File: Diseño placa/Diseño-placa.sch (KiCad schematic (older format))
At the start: 71 parts, among them M0 DIL24, M1 DIL24, M2 DIL16, SW1 SW_PUSH, SW2 SW_PUSH, SW3 SW_PUSH, SW4 SW_PUSH, SW5 SW_PUSH, U1 OPA625, U2 OPA625, U3 OPA625, U4 OPA625, U5 OPA625, U6 OPA625, X1 16M

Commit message: Más esquemático Kicad
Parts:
- added C28: 0.1u, symbol C
- added C29: 10n, symbol C
- added C30: 10u, symbol CP1
- added P1: CONN_02X08, symbol CONN_02X08
- added P?: CONN_01X01, symbol CONN_01X01
- added RV1: POT, symbol POT
- added U? (x2): REG104, symbol REG104
- gave numbers to parts that had none: 1
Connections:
- net VCC is gone; now on net GND: C11.2, C12.1, C15.1, C17.2, C22.2, C25.2, C4.1, DS1.2 (VDD), IC?.10 (VCC), IC?.30 (AVCC), M0.24 (P24), M1.24 (P24), M2.16, R27.1, R28.1
- net GND: now also DS1.15 (LED+), DS1.16 (LED-), C28.2, C29.2, C30.1, C30.2, RV1.1, RV1.2, RV1.3, U?.1 (OUT), U?.1 (OUT), U?.3 (GND), U?.3 (GND)
- net LCDE: now also DS1.6 (E)
- net LCDRS: now also DS1.4 (RS)
- net LCDRW: now also DS1.5 (R/W)
- net E15: now reaches M0.16 (P16)
- net E15: now also M1.16 (P16), P1.16 (P16)
- net E14: now reaches M0.17 (P17)
- net E14: now also M1.17 (P17), P1.14 (P14)
- net E13: now reaches M0.18 (P18)
- net E13: now also M1.18 (P18), P1.12 (P12)
- net E12: now reaches M0.19 (P19)
- net E12: now also M1.19 (P19), P1.10 (P10)
- net E7: now reaches M0.2 (P2)
- net E7: now also M1.2 (P2), P1.1 (P1)
- net E11: now reaches M0.20 (P20)
- net E11: now also M1.20 (P20), P1.8 (P8)
- net E10: now reaches M0.21 (P21)
- net E10: now also M1.21 (P21), P1.6 (P6)
- net E9: now reaches M0.22 (P22)
- net E9: now also M1.22 (P22), P1.4 (P4)
- net E8: now reaches M0.23 (P23)
- net E8: now also M1.23 (P23), P1.2 (P2)
- net E6: now reaches M0.3 (P3)
- net E6: now also M1.3 (P3), P1.3 (P3)
- net E5: now reaches M0.4 (P4)
- net E5: now also M1.4 (P4), P1.5 (P5)
- net E4: now reaches M0.5 (P5)
- net E4: now also M1.5 (P5), P1.7 (P7)
- net E3: now reaches M0.6 (P6)
- net E3: now also M1.6 (P6), P1.9 (P9)
- net E2: now reaches M0.7 (P7)
- net E2: now also M1.7 (P7), P1.11 (P11)
- net E1: now reaches M0.8 (P8)
- net E1: now also M1.8 (P8), P1.13 (P13)
- net E0: now reaches M0.9 (P9)
- net E0: now also M1.9 (P9), P1.15 (P15)
- new net: C29.1, U?.2 (NR), U?.2 (NR)
- new net: C28.1, P?.1 (P1), U?.4 (ENABLE), U?.4 (ENABLE), U?.5 (IN), U?.5 (IN)

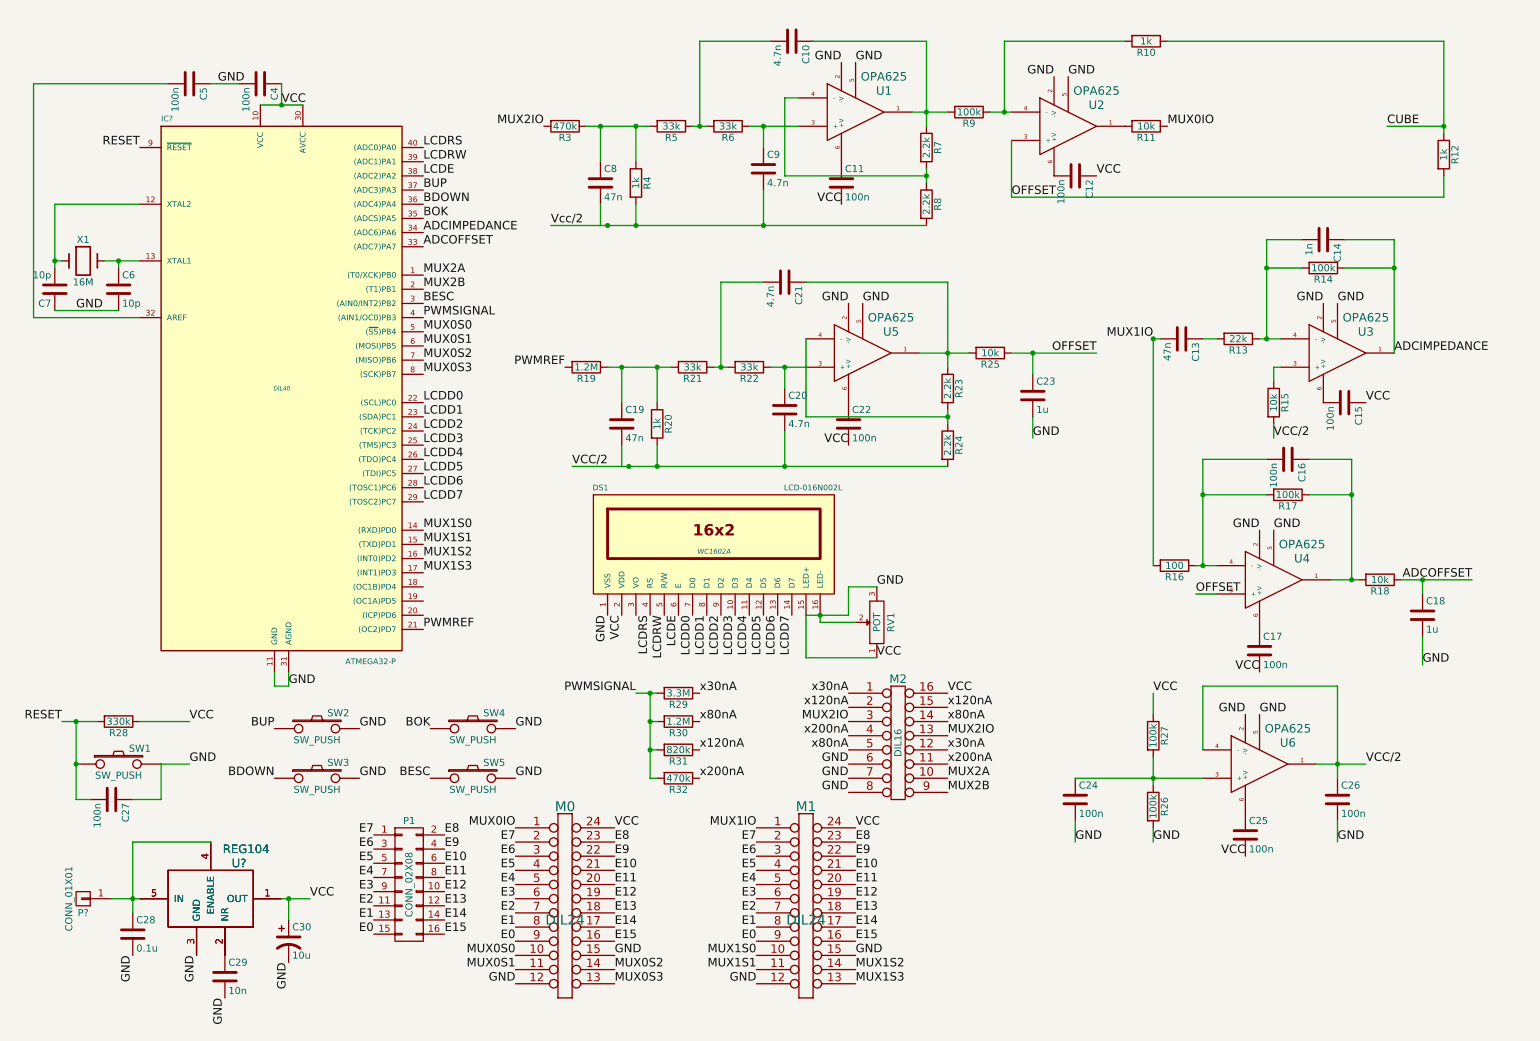
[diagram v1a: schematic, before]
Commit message: Correcciones esquemático y asociación de componentes Kicad
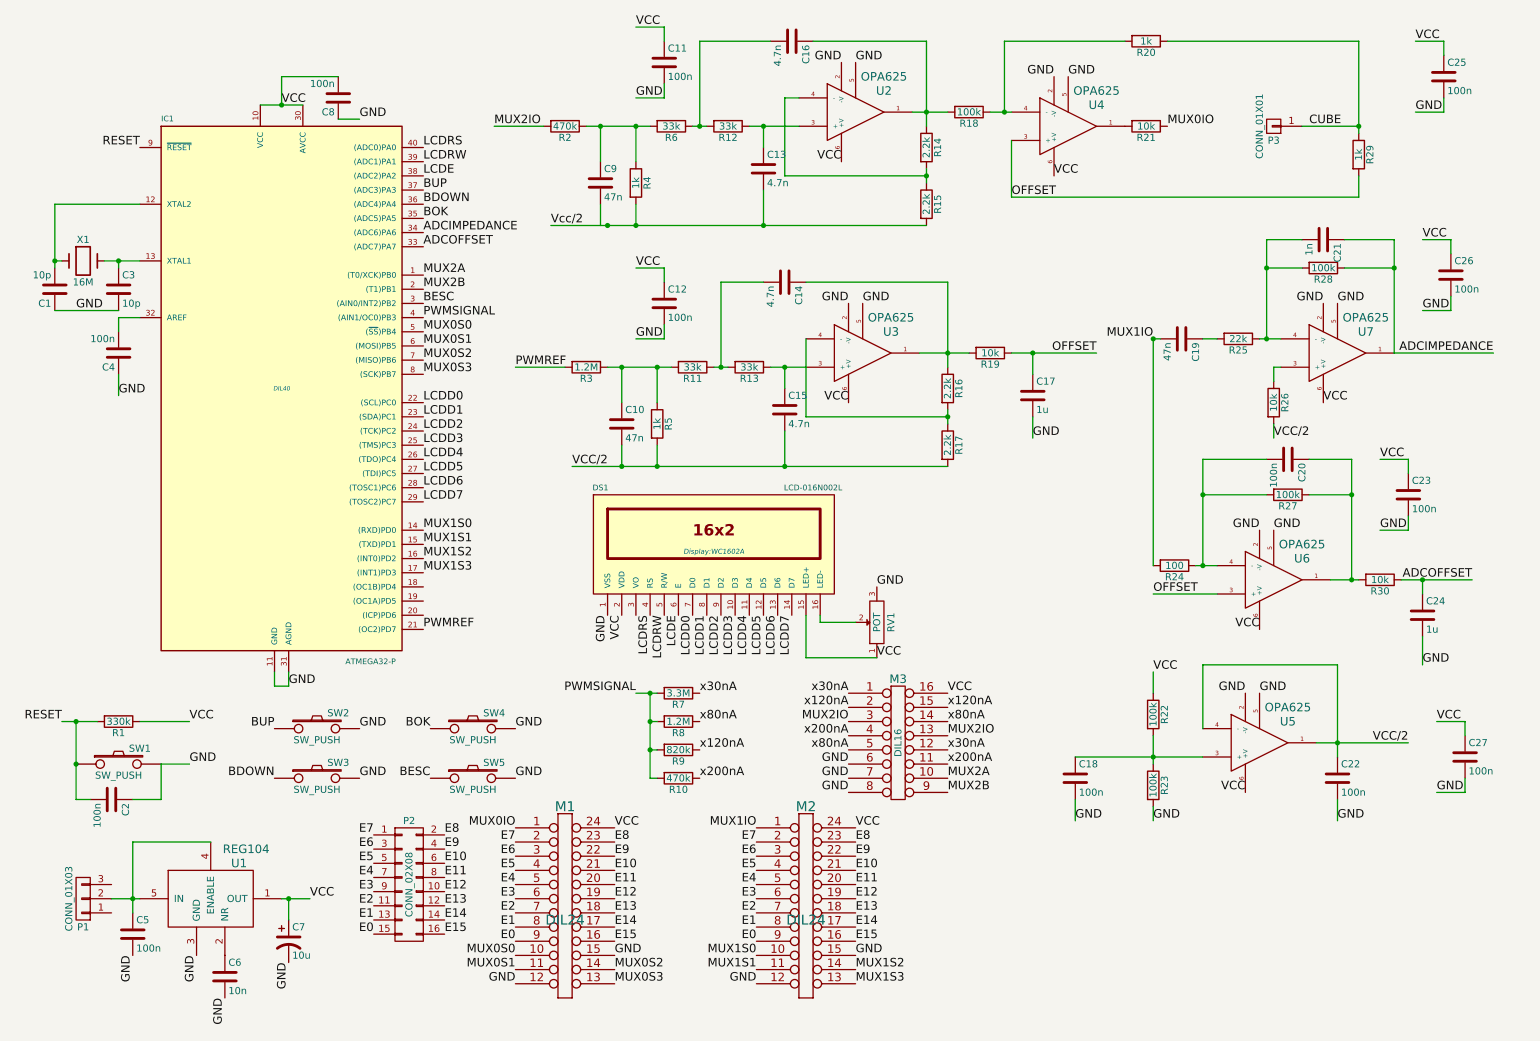
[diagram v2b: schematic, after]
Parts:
- removed C15, C17, C22: 100n, symbol C
- removed P?: CONN_01X01, symbol CONN_01X01
- removed U?: REG104, symbol REG104
- added C23, C26, C27: 100n, Capacitors_ThroughHole:C_Rect_L4_W2.5_P2.5, symbol C
- added P1: CONN_01X03, Pin_Headers:Pin_Header_Straight_1x03, symbol CONN_01X03
- added P3: CONN_01X01, Pin_Headers:Pin_Header_Straight_1x01, symbol CONN_01X01
- C1: renamed from C7; footprint (none) -> Capacitors_ThroughHole:C_Rect_L4_W2.5_P2.5
- C10: renamed from C19; footprint (none) -> Capacitors_ThroughHole:C_Rect_L4_W2.5_P2.5
- C11, C12, C25: footprint (none) -> Capacitors_ThroughHole:C_Rect_L4_W2.5_P2.5
- C13: renamed from C9; footprint (none) -> Capacitors_ThroughHole:C_Rect_L4_W2.5_P2.5
- C14: renamed from C21; footprint (none) -> Capacitors_ThroughHole:C_Rect_L4_W2.5_P2.5
- C15: renamed from C20; footprint (none) -> Capacitors_ThroughHole:C_Rect_L4_W2.5_P2.5
- C16: renamed from C10; footprint (none) -> Capacitors_ThroughHole:C_Rect_L4_W2.5_P2.5
- C17: renamed from C23; footprint (none) -> Capacitors_ThroughHole:C_Rect_L7_W6_P5
- C18: renamed from C24; footprint (none) -> Capacitors_ThroughHole:C_Rect_L4_W2.5_P2.5
- C19: renamed from C13; footprint (none) -> Capacitors_ThroughHole:C_Rect_L4_W2.5_P2.5
- C2: renamed from C27; footprint (none) -> Capacitors_ThroughHole:C_Rect_L4_W2.5_P2.5
- C20: renamed from C16; footprint (none) -> Capacitors_ThroughHole:C_Rect_L4_W2.5_P2.5
- C21: renamed from C14; footprint (none) -> Capacitors_ThroughHole:C_Rect_L4_W2.5_P2.5
- C22: renamed from C26; footprint (none) -> Capacitors_ThroughHole:C_Rect_L4_W2.5_P2.5
- C24: renamed from C18; footprint (none) -> Capacitors_ThroughHole:C_Rect_L7_W6_P5
- C3: renamed from C6; footprint (none) -> Capacitors_ThroughHole:C_Rect_L4_W2.5_P2.5
- C4: renamed from C5; footprint (none) -> Capacitors_ThroughHole:C_Rect_L4_W2.5_P2.5
- C5: renamed from C28; value 0.1u -> 100n; footprint (none) -> Capacitors_ThroughHole:C_Rect_L4_W2.5_P2.5
- C6: renamed from C29; footprint (none) -> Capacitors_ThroughHole:C_Rect_L4_W2.5_P2.5
- C7: renamed from C30; footprint (none) -> Capacitors_Elko_ThroughHole:Elko_vert_11.2x6.3mm_RM2.5
- C8: renamed from C4; footprint (none) -> Capacitors_ThroughHole:C_Rect_L4_W2.5_P2.5
- C9: renamed from C8; footprint (none) -> Capacitors_ThroughHole:C_Rect_L4_W2.5_P2.5
- DS1: footprint WC1602A -> Display:WC1602A
- M1: renamed from M0; footprint (none) -> Housings_SOIC:SOIC-24_7.5x15.4mm_Pitch1.27mm
- M2: renamed from M1; footprint (none) -> Housings_SOIC:SOIC-24_7.5x15.4mm_Pitch1.27mm
- P2: renamed from P1; footprint (none) -> Pin_Headers:Pin_Header_Angled_1x16
- R1: renamed from R28; footprint (none) -> Resistors_ThroughHole:Resistor_Horizontal_RM10mm
- R10: renamed from R32; footprint (none) -> Resistors_ThroughHole:Resistor_Horizontal_RM10mm
- R11: renamed from R21; footprint (none) -> Resistors_ThroughHole:Resistor_Horizontal_RM10mm
- R12: renamed from R6; footprint (none) -> Resistors_ThroughHole:Resistor_Horizontal_RM10mm
- R13: renamed from R22; footprint (none) -> Resistors_ThroughHole:Resistor_Horizontal_RM10mm
- R14: renamed from R7; footprint (none) -> Resistors_ThroughHole:Resistor_Horizontal_RM10mm
- R15: renamed from R8; footprint (none) -> Resistors_ThroughHole:Resistor_Horizontal_RM10mm
- R16: renamed from R23; footprint (none) -> Resistors_ThroughHole:Resistor_Horizontal_RM10mm
- R17: renamed from R24; footprint (none) -> Resistors_ThroughHole:Resistor_Horizontal_RM10mm
- R18: renamed from R9; footprint (none) -> Resistors_ThroughHole:Resistor_Horizontal_RM10mm
- R19: renamed from R25; footprint (none) -> Resistors_ThroughHole:Resistor_Horizontal_RM10mm
- R2: renamed from R3; footprint (none) -> Resistors_ThroughHole:Resistor_Horizontal_RM10mm
- R20: renamed from R10; footprint (none) -> Resistors_ThroughHole:Resistor_Horizontal_RM10mm
- R21: renamed from R11; footprint (none) -> Resistors_ThroughHole:Resistor_Horizontal_RM10mm
- R22: renamed from R27; footprint (none) -> Resistors_ThroughHole:Resistor_Horizontal_RM10mm
- R23: renamed from R26; footprint (none) -> Resistors_ThroughHole:Resistor_Horizontal_RM10mm
- R24: renamed from R16; footprint (none) -> Resistors_ThroughHole:Resistor_Horizontal_RM10mm
- R25: renamed from R13; footprint (none) -> Resistors_ThroughHole:Resistor_Horizontal_RM10mm
- R26: renamed from R15; footprint (none) -> Resistors_ThroughHole:Resistor_Horizontal_RM10mm
- R27: renamed from R17; footprint (none) -> Resistors_ThroughHole:Resistor_Horizontal_RM10mm
- R28: renamed from R14; footprint (none) -> Resistors_ThroughHole:Resistor_Horizontal_RM10mm
- R29: renamed from R12; footprint (none) -> Resistors_ThroughHole:Resistor_Horizontal_RM10mm
- R3: renamed from R19; footprint (none) -> Resistors_ThroughHole:Resistor_Horizontal_RM10mm
- R30: renamed from R18; footprint (none) -> Resistors_ThroughHole:Resistor_Horizontal_RM10mm
- R4: footprint (none) -> Resistors_ThroughHole:Resistor_Horizontal_RM10mm
- R5: renamed from R20; footprint (none) -> Resistors_ThroughHole:Resistor_Horizontal_RM10mm
- R6: renamed from R5; footprint (none) -> Resistors_ThroughHole:Resistor_Horizontal_RM10mm
- R7: renamed from R29; footprint (none) -> Resistors_ThroughHole:Resistor_Horizontal_RM10mm
- R8: renamed from R30; footprint (none) -> Resistors_ThroughHole:Resistor_Horizontal_RM10mm
- R9: renamed from R31; footprint (none) -> Resistors_ThroughHole:Resistor_Horizontal_RM10mm
- RV1: footprint (none) -> Pin_Headers:Pin_Header_Straight_1x03
- SW1, SW2, SW3, SW4, SW5: footprint (none) -> Buttons_Switches_ThroughHole:SW_PUSH
- U2: renamed from U1; footprint (none) -> Housings_SOT-23_SOT-143_TSOT-6:SC-70-6
- U3: renamed from U5; footprint (none) -> Housings_SOT-23_SOT-143_TSOT-6:SC-70-6
- U4: renamed from U2; footprint (none) -> Housings_SOT-23_SOT-143_TSOT-6:SC-70-6
- U5: renamed from U6; footprint (none) -> Housings_SOT-23_SOT-143_TSOT-6:SC-70-6
- U6: renamed from U4; footprint (none) -> Housings_SOT-23_SOT-143_TSOT-6:SC-70-6
- U7: renamed from U3; footprint (none) -> Housings_SOT-23_SOT-143_TSOT-6:SC-70-6
- X1: footprint (none) -> Crystals:Crystal_HC48-U_Vertical
- gave numbers to parts that had none: 2
- renumbered M2 to M3
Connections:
- net CUBE: now also P3.1 (P1)
- net GND: now also C12.2, C23.2, C26.2, C27.2; no longer C12.1, C7.1, C8.2, DS1.15 (LED+), DS1.16 (LED-), DS1.2 (VDD), IC1.10 (VCC), IC1.30 (AVCC), M1.24 (P24), M2.24 (P24), M3.16, R1.1, R22.1, RV1.1, RV1.2, U1.1 (OUT)
- net VCC/2: now also C10.2
- net VCC: now reaches C11.1, U2.6 (+V)
- net VCC: now also C12.1, C25.1, C7.1, C8.2, DS1.15 (LED+), DS1.2 (VDD), IC1.10 (VCC), IC1.30 (AVCC), M1.24 (P24), M2.24 (P24), M3.16, R1.1, R22.1, RV1.1, U1.1 (OUT), U3.6 (+V), U4.6 (+V), U5.6 (+V), U6.6 (+V), U7.6 (+V), C23.1, C26.1, C27.1
- net at C5.1, U1.4 (ENABLE), U1.5 (IN): now also P1.2 (P2)
- new net: DS1.16 (LED-), RV1.2
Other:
- moved on the sheet: C11, C18, C22, C4, C8, R22, R23, R29, U5

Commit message: Comienzo PCB
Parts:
- IC1: footprint DIL40 -> Housings_DIP:DIP-40_W15.24mm_LongPads
- M3: footprint (none) -> Housings_SOIC:SOIC-16_3.9x9.9mm_Pitch1.27mm
- U1: footprint (none) -> TO_SOT_Packages_SMD:TO-263-5Lead
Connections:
- net Vcc/2 is gone; now on net VCC/2: C13.2, R15.2, R4.2
- net GND: now also DS1.16 (LED-)
- net VCC/2: now also C9.2
- net at RV1.2: now also DS1.3 (VO); no longer DS1.16 (LED-)
- no-connect marks 0 -> 5
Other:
- moved on the sheet: RV1
